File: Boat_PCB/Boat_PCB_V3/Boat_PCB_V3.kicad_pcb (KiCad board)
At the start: 4 copper layers, 131.9 x 108.3 mm, 108 parts, among them J1 GPS M10-25Q, J10 Winch ESC, J11 12S HV tap, J12 Raspberry Pi 5 GPIO, J13 XT60 M18 ELECTRONICS, J14 XT60 M18 WINCH, J16 XT60 WINCH ESC OUT, J2 Pod tether, J3 CAN stub to VESCs, J4 SHT45 external, J5 Radar stepper motor, J6 Status LED, J7 SBUS RC receiver, J8 Hull leak left, J9 Hull leak right, Q1 P-FET 40V Rds<=10m, Q2 BSS138, U1 Teensy4.1, U10 INA228 electronics, U11 INA228 winch, U2 TCA9548A I2C mux, U3 TJA1051T/3 CAN xcvr, U4 BNO085, U5 ADXL375, U6 BMP390 breakout, U7 BH1750FVI-TR, U8 SHT45 internal, Y1 32.768kHz CL=12.5pF 50ppm

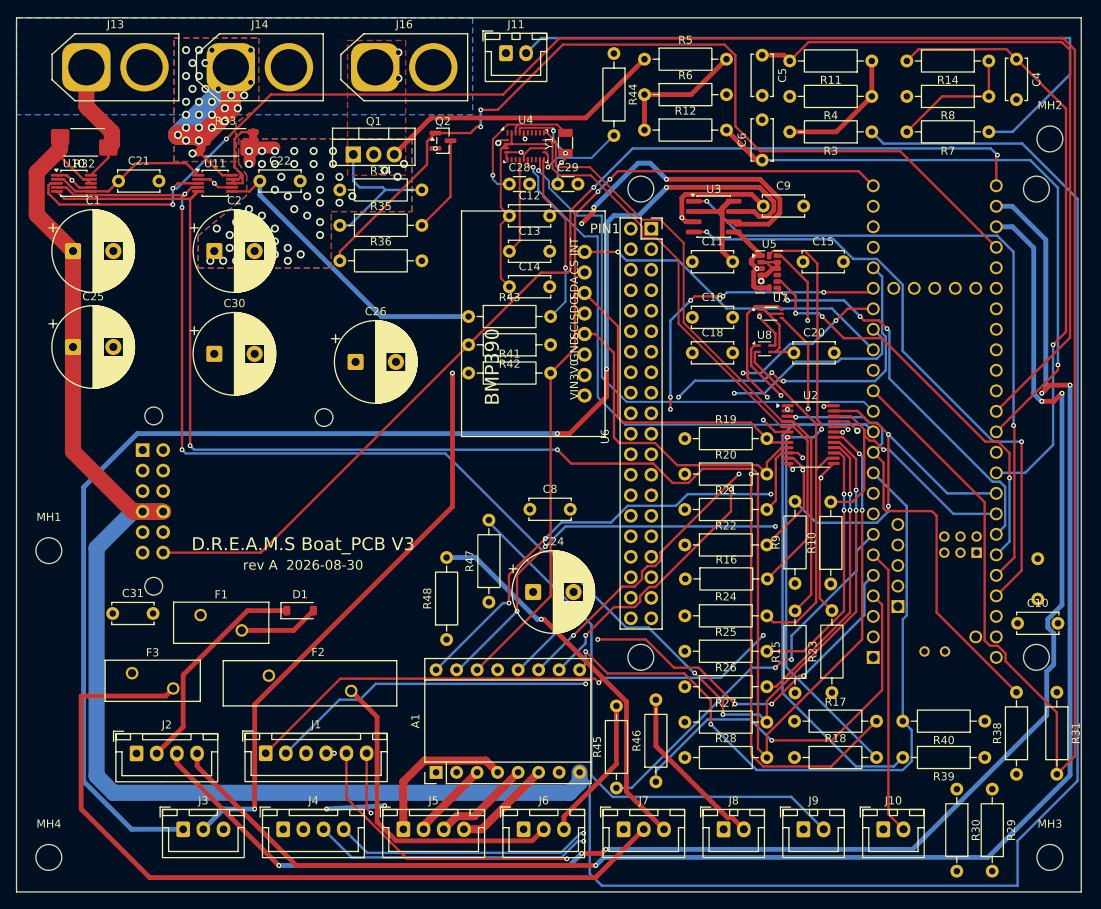
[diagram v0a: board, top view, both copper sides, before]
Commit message: feat(pcb): carrier rev D and pod board rev A
Carrier (Boat_PCB/Boat_PCB_V3), against the pre-relayout board at c4b673b:

- Re-placed and re-routed for a Pi 5 mounted face down on 30 mm
  standoffs, fully inside the outline. The board goes from 132.0 x 108.4
  to 130.6 x 101.5 mm, 7 % less area.
- Review fixes. The A2 footprint was redrawn from Pololu's drill guide:
  the old one reversed the buck's pinout end for end. XT60 pin 1 is now
  negative, J16 is an XT60-F, J11 is a JST-VH, and the Kelvin sense taps
  have their own nets. Added: TVS D3/D4/D5, gate zener D2, power and winch
  LEDs, the U12 level shifter for the WS2812, the JP1 CAN termination
  option, series resistors on off-board nets, and TP1-TP6.
- Pod tether: pack voltage through F1 (0.40 A PTC), RS-485 through U13
  (THVD2410) with R62 and R63.
- Every resistor lies flat on the 10.16 mm footprint. The edge connectors
  share one row, and the resistors sit in aligned banks.
- Parts review: the electronics and winch 68k/10k ADC dividers, with their
  1k series resistors and filter caps, only duplicated the INA228 VBUS
  readings, so they came out. R14, C8 and C10 served no purpose. That is
  11 parts removed. Teensy pins 14 and 15 are free, and the 12S tap is now
  net S12_ADC.
- ERC 70 -> 0. DRC 107 -> 0 (60 silk overlaps, 29 under-width power
  tracks, 18 silk over copper). Schematic parity 154 -> 0. Unconnected
  0 -> 0. Footprints 108 -> 126.

Pod (Boat_PCB/Pod_PCB_V3), new: schematic and a 48 x 63 mm rev A layout,
with wire-solder pads instead of connectors. ERC 0, DRC 0, parity 0.

Library: footprints and symbols for both boards, 51 footprints in all.
The A2 and Pi-socket footprints were fixed so the board copies match the
library.

Docs: CLAUDE.md baselines, the design brief, both READMEs, and the
planning docs' scope notes.

Co-Authored-By: Claude Opus 5.5 <noreply@anthropic.com>
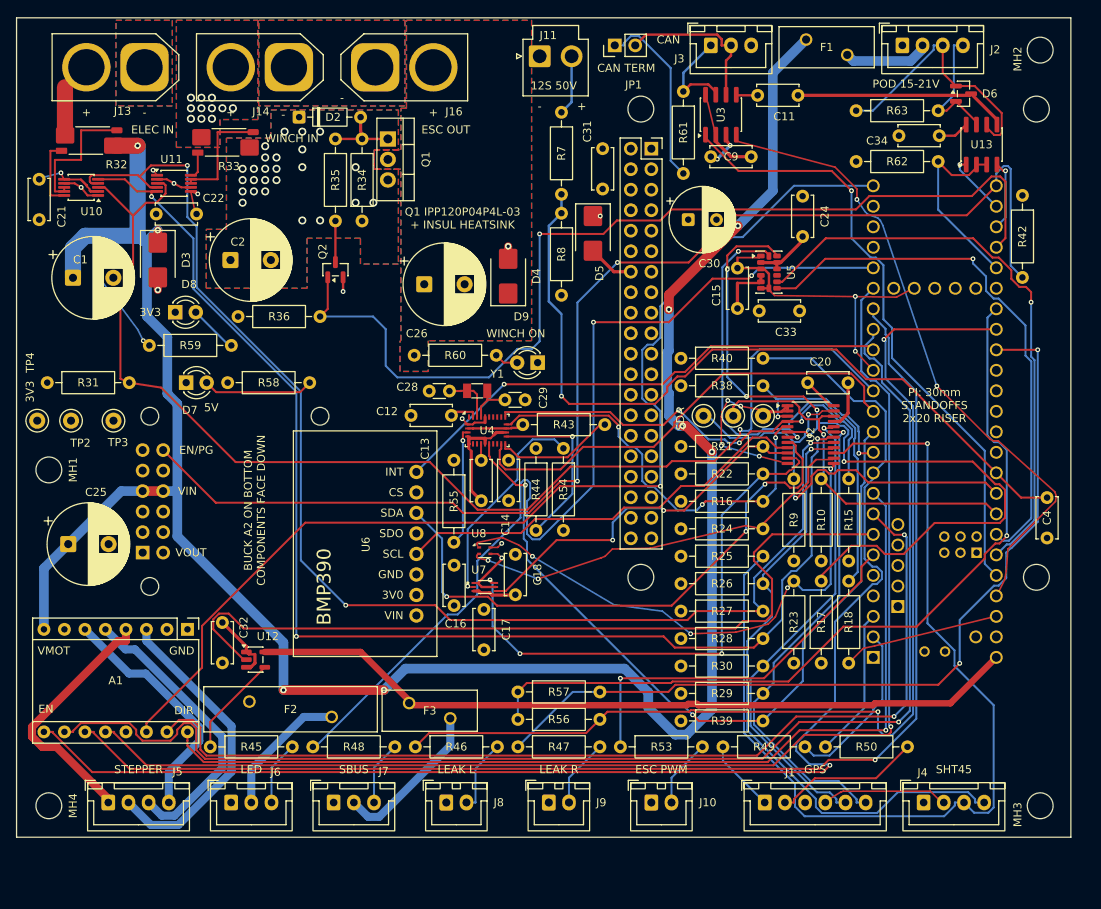
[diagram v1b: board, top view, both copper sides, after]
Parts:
- removed C10, C5, C6, C8: 100nF 50V X7R, C_Disc_D5.0mm_W2.5mm_P5.00mm
- removed D1: Schottky pod 5V, D_SOD-123
- removed R11, R12, R14: 1k 1%, R_Axial_DIN0207_L6.3mm_D2.5mm_P10.16mm_Horizontal
- removed R19, R20: 4.7k 1%, R_Axial_DIN0207_L6.3mm_D2.5mm_P10.16mm_Horizontal
- removed R3, R5: 68k 1%, R_Axial_DIN0207_L6.3mm_D2.5mm_P10.16mm_Horizontal
- removed R4, R41, R6: 10k 1%, R_Axial_DIN0207_L6.3mm_D2.5mm_P10.16mm_Horizontal
- added C32: 100nF 50V X7R, dreams_v3:C_Disc_D5.0mm_W2.5mm_P5.00mm, F.Cu at (25.5, 79.9)
- added C33: 1uF 50V X7R, dreams_v3:C_Disc_D5.0mm_W2.5mm_P5.00mm, F.Cu at (92.0, 36.3)
- added C34: 100nF 50V X7R, dreams_v3:C_Disc_D5.0mm_W2.5mm_P5.00mm, F.Cu at (114.3, 14.6)
- added D2: 1N5245B 15V, dreams_v3:D_DO-35_SOD27_P7.62mm_Horizontal, F.Cu at (35.0, 12.3)
- added D3: SMBJ24A, dreams_v3:D_SMB, F.Cu at (17.5, 30.0)
- added D4: SMBJ24A, dreams_v3:D_SMB, F.Cu at (60.9, 32.0)
- added D5: SMBJ5.0A, dreams_v3:D_SMB, F.Cu at (71.4, 26.7)
- added D6: NUP2105L, dreams_v3:SOT-23, F.Cu at (117.3, 9.40)
- added D7: green +5V, dreams_v3:LED_D3.0mm, F.Cu at (21.0, 45.2)
- added D8: green +3V3, dreams_v3:LED_D3.0mm, F.Cu at (19.7, 36.5)
- added D9: red WINCH ON, dreams_v3:LED_D3.0mm, F.Cu at (64.5, 42.7)
- added JP1: CAN TERM, dreams_v3:PinHeader_1x02_P2.54mm_Vertical, F.Cu at (74.1, 3.41)
- added R49: 1k 1%, dreams_v3:R_Axial_DIN0207_L6.3mm_D2.5mm_P10.16mm_Horizontal, F.Cu at (87.5, 90.3)
- added R50: 1k 1%, dreams_v3:R_Axial_DIN0207_L6.3mm_D2.5mm_P10.16mm_Horizontal, F.Cu at (100.2, 90.3)
- added R53: 1k 1%, dreams_v3:R_Axial_DIN0207_L6.3mm_D2.5mm_P10.16mm_Horizontal, F.Cu at (74.8, 90.3)
- added R54: 100k 1%, dreams_v3:R_Axial_DIN0207_L6.3mm_D2.5mm_P10.16mm_Horizontal, F.Cu at (67.7, 53.3)
- added R55: 10k 1%, dreams_v3:R_Axial_DIN0207_L6.3mm_D2.5mm_P10.16mm_Horizontal, F.Cu at (54.2, 54.8)
- added R56: 100k 1%, dreams_v3:R_Axial_DIN0207_L6.3mm_D2.5mm_P10.16mm_Horizontal, F.Cu at (62.1, 86.9)
- added R57: 100k 1%, dreams_v3:R_Axial_DIN0207_L6.3mm_D2.5mm_P10.16mm_Horizontal, F.Cu at (62.1, 83.5)
- added R58: 1.5k 1%, dreams_v3:R_Axial_DIN0207_L6.3mm_D2.5mm_P10.16mm_Horizontal, F.Cu at (26.1, 45.2)
- added R59: 680R 1%, dreams_v3:R_Axial_DIN0207_L6.3mm_D2.5mm_P10.16mm_Horizontal, F.Cu at (16.4, 40.6)
- added R60: 10k 1%, dreams_v3:R_Axial_DIN0207_L6.3mm_D2.5mm_P10.16mm_Horizontal, F.Cu at (49.3, 41.8)
- added R61: 120R 1%, dreams_v3:R_Axial_DIN0207_L6.3mm_D2.5mm_P10.16mm_Horizontal, F.Cu at (82.6, 9.12)
- added R62: 10k 1%, dreams_v3:R_Axial_DIN0207_L6.3mm_D2.5mm_P10.16mm_Horizontal, F.Cu at (114.2, 17.8)
- added R63: 120R 1%, dreams_v3:R_Axial_DIN0207_L6.3mm_D2.5mm_P10.16mm_Horizontal, F.Cu at (104.0, 11.5)
- added TP1: GND, dreams_v3:TestPoint_Keystone_5000-5004_Miniature, F.Cu at (92.5, 49.3)
- added TP2: GND, dreams_v3:TestPoint_Keystone_5000-5004_Miniature, F.Cu at (6.75, 49.9)
- added TP3: +5V, dreams_v3:TestPoint_Keystone_5000-5004_Miniature, F.Cu at (12.0, 49.9)
- added TP4: +3V3, dreams_v3:TestPoint_Keystone_5000-5004_Miniature, F.Cu at (2.56, 49.9)
- added TP5: SDA, dreams_v3:TestPoint_Keystone_5000-5004_Miniature, F.Cu at (85.1, 49.3)
- added TP6: SCL, dreams_v3:TestPoint_Keystone_5000-5004_Miniature, F.Cu at (88.8, 49.3)
- added U12: 74AHCT1G125, dreams_v3:SOT-23-5, F.Cu at (29.6, 79.5)
- added U13: THVD2410, dreams_v3:SOIC-8_3.9x4.9mm_P1.27mm, F.Cu at (119.5, 15.7)
- A1: footprint Pololu_Breakout-16_15.2x20.3mm -> dreams_v3:Pololu_Breakout-16_15.2x20.3mm
- A2: footprint Pololu_D36V50F5 -> dreams_v3:Pololu_D36V50F5
- C1, C2, C25, C26: footprint CP_Radial_D10.0mm_P5.00mm -> dreams_v3:CP_Radial_D10.0mm_P5.00mm
- C11, C12, C13, C14, C15, C16, C18, C20, C21, C22, C31, C4, C9: footprint C_Disc_D5.0mm_W2.5mm_P5.00mm -> dreams_v3:C_Disc_D5.0mm_W2.5mm_P5.00mm
- C17: footprint C_Disc_D5.0mm_W2.5mm_P5.00mm -> dreams_v3:C_Disc_D5.0mm_W2.5mm_P5.00mm; moved to F.Cu
- C24: value 10uF 25V -> 10uF 25V X7R; footprint CP_Radial_D10.0mm_P5.00mm -> dreams_v3:C_Disc_D5.0mm_W2.5mm_P5.00mm
- C28, C29: footprint C_Disc_D3.0mm_W1.6mm_P2.50mm -> dreams_v3:C_Disc_D3.0mm_W1.6mm_P2.50mm
- C30: value 470uF 35V -> 470uF 16V low-ESR 105C; footprint CP_Radial_D10.0mm_P5.00mm -> dreams_v3:CP_Radial_D8.0mm_P3.50mm
- F1: value PTC 0.75A hold -> PTC 0.40A hold; footprint Fuse_BelFuse_0ZRE0075FF_L11.5mm_W4.8mm -> dreams_v3:Fuse_BelFuse_0ZRE0075FF_L11.5mm_W4.8mm
- F2: footprint Fuse_BelFuse_0ZRE0125FF_L21.2mm_W5.3mm -> dreams_v3:Fuse_BelFuse_0ZRE0125FF_L21.2mm_W5.3mm
- F3: footprint Fuse_BelFuse_0ZRE0075FF_L11.5mm_W4.8mm -> dreams_v3:Fuse_BelFuse_0ZRE0075FF_L11.5mm_W4.8mm
- J1: footprint JST_XH_B6B-XH-A_1x06_P2.50mm_Vertical -> dreams_v3:JST_XH_B6B-XH-A_1x06_P2.50mm_Vertical
- J10, J8, J9: footprint JST_XH_B2B-XH-A_1x02_P2.50mm_Vertical -> dreams_v3:JST_XH_B2B-XH-A_1x02_P2.50mm_Vertical
- J11: value 12S HV tap -> 12S HV tap (JST-VH); footprint JST_XH_B2B-XH-A_1x02_P2.50mm_Vertical -> dreams_v3:JST_VH_B2P-VH_1x02_P3.96mm_Vertical
- J12: footprint RaspberryPi_5_GPIO_Socket_2x20 -> dreams_v3:RaspberryPi_5_GPIO_Socket_2x20
- J13, J14: footprint AMASS_XT60-M_1x02_P7.20mm_Vertical -> dreams_v3:AMASS_XT60-M_1x02_P7.20mm_Vertical
- J16: value XT60 WINCH ESC OUT -> XT60-F WINCH ESC OUT (female); footprint AMASS_XT60-M_1x02_P7.20mm_Vertical -> dreams_v3:AMASS_XT60-F_1x02_P7.20mm_Vertical
- J2, J4, J5: footprint JST_XH_B4B-XH-A_1x04_P2.50mm_Vertical -> dreams_v3:JST_XH_B4B-XH-A_1x04_P2.50mm_Vertical
- J3, J6, J7: footprint JST_XH_B3B-XH-A_1x03_P2.50mm_Vertical -> dreams_v3:JST_XH_B3B-XH-A_1x03_P2.50mm_Vertical
- MH1, MH2, MH3, MH4: value MountingHole_3.2mm_M3 -> MountingHole; footprint MountingHole_3.2mm_M3 -> dreams_v3:MountingHole_3.2mm_M3
- Q1: value P-FET 40V Rds<=10m -> IPP120P04P4L-03; footprint TO-220-3_Vertical -> dreams_v3:TO-220-3_Vertical
- Q2: footprint SOT-23 -> dreams_v3:SOT-23
- R10, R15, R16, R17, R18, R21, R22, R23, R24, R25, R26, R27, R28, R29, R30, R31, R34, R35, R36, R38, R39, R40, R42, R43, R44, R45, R46, R47, R48, R7, R8, R9: footprint R_Axial_DIN0207_L6.3mm_D2.5mm_P10.16mm_Horizontal -> dreams_v3:R_Axial_DIN0207_L6.3mm_D2.5mm_P10.16mm_Horizontal
- R32, R33: footprint R_Shunt_Vishay_WSK2512_6332Metric_T1.19mm -> dreams_v3:R_Shunt_Vishay_WSK2512_6332Metric_T1.19mm
- U1: footprint Teensy41 -> dreams_v3:Teensy41
- U10, U11: footprint MSOP-10_3x3mm_P0.5mm -> dreams_v3:MSOP-10_3x3mm_P0.5mm
- U2: footprint TSSOP-24_4.4x7.8mm_P0.65mm -> dreams_v3:TSSOP-24_4.4x7.8mm_P0.65mm
- U3: footprint SOIC-8_3.9x4.9mm_P1.27mm -> dreams_v3:SOIC-8_3.9x4.9mm_P1.27mm
- U4: footprint LGA-28_5.2x3.8mm_P0.5mm -> dreams_v3:LGA-28_5.2x3.8mm_P0.5mm
- U5: footprint LGA-14_3x5mm_P0.8mm_LayoutBorder1x6y -> dreams_v3:LGA-14_3x5mm_P0.8mm_LayoutBorder1x6y
- U6: footprint BMP390 -> dreams_v3:BMP390
- U7: footprint XDCR_BH1750FVI-TR -> dreams_v3:XDCR_BH1750FVI-TR
- U8: footprint Sensirion_DFN-4_1.5x1.5mm_P0.8mm_SHT4x_NoCentralPad -> dreams_v3:Sensirion_DFN-4_1.5x1.5mm_P0.8mm_SHT4x_NoCentralPad
- Y1: footprint Crystal_SMD_3215-2Pin_3.2x1.5mm -> dreams_v3:Crystal_SMD_3215-2Pin_3.2x1.5mm
- moved R31 130.8 mm to (3.80, 45.2), turned to 0 degrees
- moved J2 129.2 mm to (109.7, 3.41)
- moved J3 117.1 mm to (86.0, 3.41)
- moved F1 103.5 mm to (97.8, 2.69)
- moved C31 83.7 mm to (72.6, 16.2), turned to -90 degrees
- moved J4 79.4 mm to (112.4, 97.2)
- moved C17 68.9 mm to (57.9, 73.3)
- moved R38 63.6 mm to (82.3, 45.6), turned to 0 degrees
- moved J1 62.1 mm to (92.7, 97.2)
- moved R42 61.3 mm to (124.6, 22.0), turned to -90 degrees
- moved C30 61.0 mm to (83.2, 25.0)
- moved C24 59.3 mm to (97.4, 22.1), turned to -90 degrees
- moved R40 58.6 mm to (82.3, 42.2), turned to 0 degrees
- moved R8 54.9 mm to (67.5, 24.2), turned to -90 degrees
- moved C4 54.4 mm to (127.7, 59.4)
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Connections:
- F1 pad 1: +5V -> /+VELEC
- F1 pad 2: /POD_5V_F -> /POD_VPACK
- J1 pad 1: /GPS_TX -> /GPS_TX_EXT
- J1 pad 2: /GPS_RX -> /GPS_RX_EXT
- J10 pad 2: /WINCH_PWM -> /WINCH_PWM_EXT
- J13 pad 1: /SH_ELEC_P -> GND
- J13 pad 2: GND -> /SH_ELEC_P
- J14 pad 1: /SH_WINCH_P -> GND
- J14 pad 2: GND -> /SH_WINCH_P
- J16 pad 1: /WINCH_SW -> GND
- J16 pad 2: GND -> /WINCH_SW
- J2 pad 2: /POD_5V -> /POD_VPACK
- R32 pad 2: /SH_ELEC_P -> /ELEC_SHUNT_P
- R32 pad 3: /+VELEC -> /ELEC_SHUNT_N
- R33 pad 2: /SH_WINCH_P -> /WINCH_SHUNT_P
- R33 pad 3: /+VWINCH -> /WINCH_SHUNT_N
- R45 pad 1: /LED_DIN -> /LED_DIN_5V
- R7 pad 2: /S12_SENSE -> /S12_ADC
- R8 pad 1: /S12_SENSE -> /S12_ADC
- U1 pad 26: /TETHER_B -> /TETHER_RX
- U1 pad 27: /TETHER_A -> /TETHER_TX
- U1 pad 29: unconnected-(U1-37_CS-Pad29) -> /TETHER_DE
- U1 pad 31: unconnected-(U1-39_MISO1_OUT1A-Pad31) -> /LEAK_EXC
- U1 pad 32: unconnected-(U1-40_A16-Pad32) -> /LEAK_L
- U1 pad 33: unconnected-(U1-41_A17-Pad33) -> /LEAK_R
- U1 pad 36: /ELEC_ADC -> unconnected-(U1-14_A0_TX3_SPDIF_OUT-Pad36)
- U1 pad 37: /WINCH_ADC -> unconnected-(U1-15_A1_RX3_SPDIF_IN-Pad37)
- U1 pad 4: /LEAK_L -> unconnected-(U1-2_OUT2-Pad4)
- U1 pad 5: /LEAK_R -> unconnected-(U1-3_LRCLK2-Pad5)
- U10 pad 10: /SH_ELEC_P -> /ELEC_SHUNT_P
- U10 pad 8: /+VELEC -> /ELEC_SHUNT_N
- U10 pad 9: /+VELEC -> /ELEC_SHUNT_N
- U11 pad 10: /SH_WINCH_P -> /WINCH_SHUNT_P
- U11 pad 8: /+VWINCH -> /WINCH_SHUNT_N
- U11 pad 9: /+VWINCH -> /WINCH_SHUNT_N
- U4 pad 4: +3V3 -> /IMU_BOOTN
- U7 pad 2: GND -> /BH_ADDR
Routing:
- net /TETHER_B: track 198.7 -> 16.6 mm, vias 3 -> 0
- net /CANH: track 172.1 -> 12.2 mm, vias 3 -> 0
- net /TETHER_A: track 191.3 -> 32.4 mm, vias 5 -> 0
- net /INA_ALERT: track 291.7 -> 149.7 mm, vias 3 -> 1
- net +3V3: track 244.2 -> 125.9 mm, vias 5 -> 8
- net /CANL: track 137.1 -> 19.8 mm, vias 5 -> 0
- net /LEAK_EXC: track 0.00 -> 102.3 mm, vias 0 -> 1
- net /STEP_MS1: track 69.0 -> 163.9 mm, vias 3 -> 1
- net /CH7_SDA: track 153.1 -> 60.1 mm, vias 2 -> 1
- net /STEP_MS2: track 68.2 -> 160.5 mm, vias 4 -> 1
- net /CH7_SCL: track 147.4 -> 59.1 mm, vias 2 -> 1
- net /ELEC_ADC: track 88.3 -> 0.00 mm
- net GND: track 50.5 -> 135.4 mm
- net /STEP_EN: track 89.3 -> 171.7 mm, vias 2 -> 1
- net /SBUS_5V: track 101.5 -> 19.7 mm
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- added copper zone on B.Cu, net /WINCH_SW
- added copper zone on F.Cu, net GND
- removed copper zone on In2.Cu, net /WINCH_SW
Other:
- board size 131.9 x 108.3 mm -> 130.6 x 101.5 mm
- board text added: "+"
- board text added: "-"
- board text added: "12S 50V"
- board text added: "3V3"
- board text added: "5V"
- board text added: "BUCK A2 ON BOTTOM COMPONENTS FACE DOWN"
- board text added: "CAN"
- board text added: "CAN TERM"
- board text added: "CUT TEENSY VIN-VUSB BEFORE FITTING"
- board text added: "DIR"
- board text added: "ELEC IN"
- board text added: "ELEC PACK FUSE 5A MAX"
- board text added: "EN"
- board text added: "EN/PG"
- board text added: "ESC OUT"
- board text added: "ESC PWM"
- board text added: "GND"
- board text added: "GPS"
- board text added: "JLCJLCJLCJLC"
- board text added: "LEAK L"
- board text added: "LEAK R"
- board text added: "LED"
- board text added: "PI: 30mm STANDOFFS 2x20 RISER"
- board text added: "POD 15-21V"
- board text added: "Pi 5 body, FACE DOWN on 30 mm standoffs (outline from J12's holes)"
- board text added: "Pi USB/RJ45 end: parts below this line must stay < 10 mm tall"
- board text added: "Q1 IPP120P04P4L-03 + INSUL HEATSINK"
- board text added: "Q1 heatsink keep-out (insulated clip-on)"
- board text added: "SBUS"
- board text added: "SCL"
- board text added: "SDA"
- board text added: "SHT45"
- board text added: "STEPPER"
- board text added: "VIN"
- board text added: "VMOT"
- board text added: "VOUT"
- board text added: "WINCH IN"
- board text added: "WINCH ON"
- board text added: "rev D 2026-09-28"
- board text removed: "Pi 5 body 56 x 85 - keep tall parts off the front here"
- board text removed: "rev A 2026-08-30"
